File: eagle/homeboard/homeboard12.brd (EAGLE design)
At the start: 100 x 80 mm, 115 parts, among them IC1 XCF02S, IC2 25LC080SN, IC3 ATMEGA32U2-TQFP, Q5 BC848SMD, Q6 BC848SMD, Q7 BC848SMD, Q8 BC848SMD, T1 BSS138, T2 BC848, T3 BSS138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

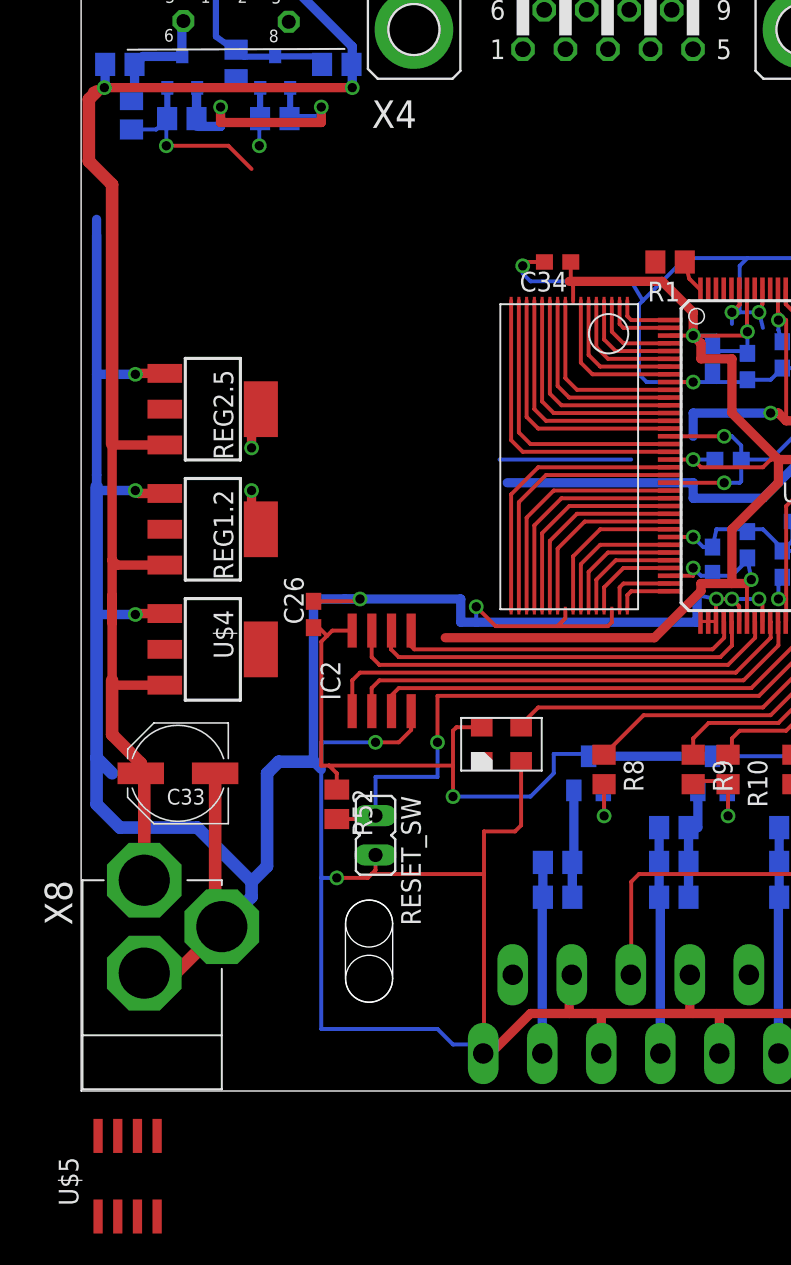
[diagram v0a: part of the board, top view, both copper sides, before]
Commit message: re-added mc33269
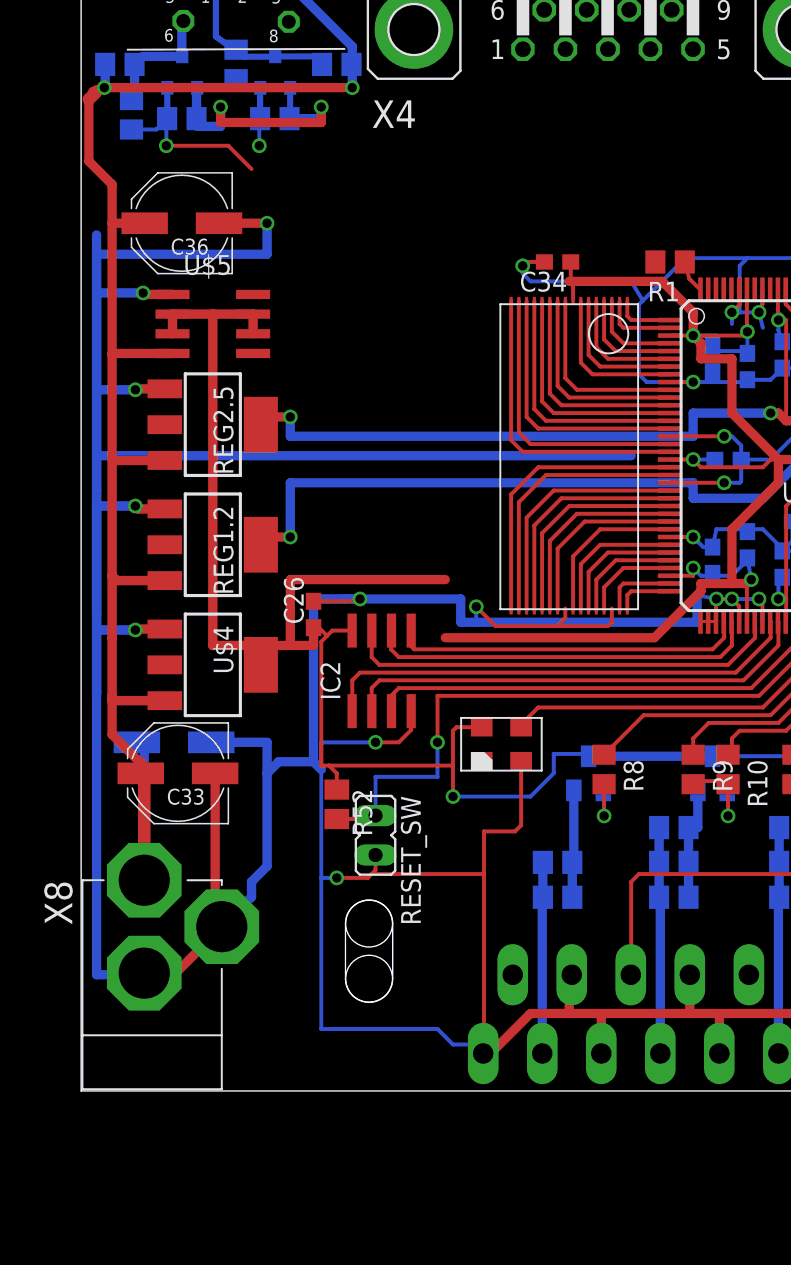
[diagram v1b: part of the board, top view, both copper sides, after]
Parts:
- added C35, C36: 100u, rcl:PANASONIC_D
- moved U$5 55.3 mm to (8.50, 49.5), turned to 270 degrees
- moved REG1.2 1.00 mm to (8.50, 35.2)
- moved REG2.5 1.00 mm to (8.50, 43.0)
- moved U$4 1.00 mm to (8.50, 27.5)
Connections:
- net GND: now also C35.-, C36.-, U$5.1
- net VCC: now also U$5.2, U$5.3, U$5.6, U$5.7
- net VCC5: now also C35.+, C36.+, U$5.4
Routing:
- net VCC: track 359.7 -> 412.0 mm
- net GND: track 650.9 -> 700.8 mm, vias 35 -> 37
- net VCCAUX: track 82.5 -> 110.5 mm
- net VCCINT: track 80.6 -> 99.0 mm
- net VCC5: track 92.1 -> 105.8 mm

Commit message: tidying up
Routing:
- net VCC: track 412.0 -> 412.4 mm, vias 25 -> 21
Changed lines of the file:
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@@
 <wire x1="29" y1="19" x2="30.5" y2="20.5" width="0.254" layer="16"/>
 <wire x1="30.5" y1="20.5" x2="30.5" y2="21.75" width="0.254" layer="16"/>
-<wire x1="30.5" y1="21.75" x2="32.5" y2="21.75" width="0.254" layer="16"/>
+<wire x1="30.5" y1="21.75" x2="32.6" y2="21.75" width="0.254" layer="16"/>
 <wire x1="16.5" y1="19.45" x2="16.5" y2="20.5" width="0.254" layer="1"/>
 <wire x1="16.5" y1="20.5" x2="16" y2="21" width="0.254" layer="1"/>
@@
 <via x="51.5" y="40.75" extent="1-16" drill="0.6" shape="square"/>
 <wire x1="45" y1="40.75" x2="46.5" y2="40.75" width="0.6" layer="1"/>
-<wire x1="46.5" y1="40.75" x2="51" y2="40.75" width="0.6" layer="1"/>
-<wire x1="51" y1="40.75" x2="51.5" y2="40.75" width="0.6" layer="1"/>
+<wire x1="46.5" y1="40.75" x2="51.5" y2="40.75" width="0.6" layer="1"/>
 <wire x1="53.5" y1="40.75" x2="53.5" y2="41.25" width="0.254" layer="16"/>
-<wire x1="53.5" y1="41.25" x2="56.5" y2="41.25" width="0.254" layer="16"/>
+<wire x1="53.5" y1="41.25" x2="56" y2="41.25" width="0.254" layer="16"/>
+<wire x1="56" y1="41.25" x2="56.5" y2="41.25" width="0.254" layer="16"/>
 <wire x1="56.5" y1="41.25" x2="57.75" y2="41.25" width="0.254" layer="16"/>
 <wire x1="56.4" y1="41.35" x2="56.5" y2="41.25" width="0.254" layer="16"/>
 <wire x1="51.5" y1="40.75" x2="53.5" y2="40.75" width="0.6" layer="16"/>
-<via x="51.5" y="41.75" extent="1-16" drill="0.6" shape="square"/>
-<wire x1="51.5" y1="41.75" x2="51" y2="40.75" width="0.6" layer="1"/>
-<via x="51.5" y="39.75" extent="1-16" drill="0.6" shape="square"/>
-<wire x1="51.5" y1="39.75" x2="51" y2="40.75" width="0.6" layer="1"/>
-<via x="53.5" y="41.75" extent="1-16" drill="0.6" shape="square"/>
-<wire x1="53.5" y1="41.75" x2="53.5" y2="42.25" width="0.6" layer="1"/>
 <wire x1="53.5" y1="42.25" x2="54.25" y2="43" width="0.6" layer="1"/>
 <wire x1="54.25" y1="43" x2="54.25" y2="49" width="0.6" layer="1"/>
 <wire x1="54.25" y1="49" x2="53.75" y2="49" width="0.6" layer="1"/>
-<via x="53.5" y="39.75" extent="1-16" drill="0.6" shape="square"/>
-<wire x1="53.5" y1="39.75" x2="54.5" y2="38.75" width="0.6" layer="1"/>
-<wire x1="54.5" y1="38.75" x2="54.5" y2="33" width="0.6" layer="1"/>
+<wire x1="54.5" y1="38.75" x2="54.5" y2="38.5" width="0.6" layer="1"/>
+<wire x1="54.5" y1="38.5" x2="54.5" y2="33" width="0.6" layer="1"/>
 <wire x1="54.5" y1="33" x2="54.75" y2="32.75" width="0.6" layer="1"/>
-<wire x1="53.5" y1="39.75" x2="53.5" y2="40.75" width="0.6" layer="1"/>
 <via x="53.5" y="40.75" extent="1-16" drill="0.6" shape="square"/>
-<wire x1="53.5" y1="40.75" x2="53.5" y2="41.75" width="0.6" layer="1"/>
-<wire x1="51.5" y1="39.75" x2="53.5" y2="39.75" width="0.6" layer="16"/>
-<wire x1="51.5" y1="41.75" x2="53.5" y2="41.75" width="0.6" layer="16"/>
-<wire x1="53.5" y1="41.75" x2="53.5" y2="39.75" width="0.6" layer="16"/>
 <wire x1="57.75" y1="48.25" x2="57.75" y2="48.75" width="0.6" layer="1"/>
 <wire x1="57.75" y1="48.75" x2="57.75" y2="50" width="0.6" layer="1"/>
@@
 <wire x1="11.625" y1="28.75" x2="11.625" y2="28.375" width="0.6" layer="1"/>
 <wire x1="16.2109125" y1="29.7109125" x2="15.875" y2="29.375" width="0.254" layer="1"/>
+<wire x1="53.5" y1="40.75" x2="53.5" y2="39.5" width="0.6" layer="1"/>
+<wire x1="53.5" y1="39.5" x2="54.5" y2="38.5" width="0.6" layer="1"/>
+<wire x1="53.5" y1="42.25" x2="53.5" y2="40.75" width="0.6" layer="1"/>
+<wire x1="47.6" y1="39.65" x2="47.6" y2="36.75" width="0.254" layer="16"/>
+<wire x1="47.6" y1="36.75" x2="48.5" y2="36.75" width="0.254" layer="16"/>
+<wire x1="54" y1="33.25" x2="54" y2="33.9" width="0.254" layer="16"/>
+<wire x1="54" y1="33.9" x2="54.25" y2="34.15" width="0.254" layer="16"/>
+<wire x1="56.5" y1="33.9" x2="54.5" y2="33.9" width="0.254" layer="16"/>
+<wire x1="54.5" y1="33.9" x2="54.25" y2="34.15" width="0.254" layer="16"/>
+<wire x1="56" y1="41.35" x2="56" y2="41.25" width="0.254" layer="16"/>
+<wire x1="48" y1="44.75" x2="48.1" y2="44.75" width="0.254" layer="16"/>
+<wire x1="43" y1="47.6" x2="43" y2="47.75" width="0.254" layer="16"/>
+<wire x1="40.75" y1="48.5" x2="40.75" y2="48.1" width="0.254" layer="16"/>
 <wire x1="77.5" y1="64.0426" x2="76.7" y2="64.0426" width="0" layer="19" extent="1-1"/>
 <wire x1="75.2074" y1="60.15" x2="76.7" y2="64.0426" width="0" layer="19" extent="1-1"/>
 <wire x1="75.5" y1="52.25" x2="75.2074" y2="60.15" width="0" layer="19" extent="1-1"/>
-<wire x1="48.1" y1="44.75" x2="48" y2="44.75" width="0" layer="19" extent="16-16"/>
-<wire x1="43" y1="47.6" x2="43" y2="47.75" width="0" layer="19" extent="16-16"/>
-<wire x1="75.5" y1="29.25" x2="75.393396875" y2="29.087409375" width="0" layer="19" extent="1-1"/>
-<wire x1="32.5" y1="21.75" x2="32.75" y2="21.6" width="0" layer="19" extent="16-16"/>
-<wire x1="56" y1="41.35" x2="56.4" y2="41.35" width="0" layer="19" extent="16-16"/>
-<wire x1="40.75" y1="48.1" x2="40.75" y2="48.5" width="0" layer="19" extent="16-16"/>
-<wire x1="56.5" y1="33.9" x2="56" y2="33.75" width="0" layer="19" extent="16-16"/>
-<wire x1="54.25" y1="34.15" x2="54" y2="33.25" width="0" layer="19" extent="16-16"/>
-<wire x1="47.6" y1="36.75" x2="47.6" y2="39.65" width="0" layer="19" extent="16-16"/>
-<wire x1="48.5" y1="36.75" x2="47.6" y2="36.75" width="0" layer="19" extent="16-16"/>
 <wire x1="87.15" y1="31.5" x2="77" y2="27.75" width="0" layer="19" extent="1-1"/>
 <wire x1="86.65" y1="35.5" x2="87.15" y2="31.5" width="0" layer="19" extent="1-1"/>
@@
 <wire x1="92.95" y1="10.5" x2="98.45" y2="24" width="0" layer="19" extent="1-16"/>
 <wire x1="91.4" y1="7" x2="92.95" y2="10.5" width="0" layer="19" extent="1-16"/>
+<wire x1="32.6" y1="21.75" x2="32.75" y2="21.6" width="0.254" layer="16"/>
+<wire x1="75.393396875" y1="29.087409375" x2="75.393396875" y2="29.143396875" width="0.254" layer="1"/>
+<wire x1="75.393396875" y1="29.143396875" x2="75.5" y2="29.25" width="0.254" layer="1"/>
 </signal>
 <signal name="TCK">
@@
 <wire x1="44" y1="24.75" x2="29.5" y2="24.75" width="0.254" layer="1"/>
 <wire x1="29.5" y1="24.75" x2="28.5" y2="23.75" width="0.254" layer="1"/>
-<wire x1="28.5" y1="23.25" x2="28.5" y2="23.75" width="0.254" layer="1"/>
-<wire x1="28.5" y1="23.25" x2="28.395" y2="23.475" width="0" layer="19" extent="1-1"/>
+<wire x1="28.5" y1="23.25" x2="28.5" y2="23.5" width="0.254" layer="1"/>
+<wire x1="28.5" y1="23.5" x2="28.5" y2="23.75" width="0.254" layer="1"/>
+<wire x1="28.395" y1="23.475" x2="28.475" y2="23.475" width="0.254" layer="1"/>
+<wire x1="28.475" y1="23.475" x2="28.5" y2="23.5" width="0.254" layer="1"/>
 </signal>
 <signal name="XXB1">
